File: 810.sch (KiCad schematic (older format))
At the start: 327 parts, among them J1 PJ301BM, J10 PJ301BM, J11 PJ301BM, J12 PJ301BM, J13 PJ301BM, J14 PJ301BM, J15 JACK_MONO_SW, J16 PJ301BM, J17 PJ301B, J18 PJ301B, J2 PJ301BM, J3 PJ301BM, J4 PJ301B, J5 PJ301B, J6 PJ301BM, J7 PJ301BM, J8 PJ301BM, J9 PJ301BM, P1 CONN_01X08, P2 CONN_02X05, P3 CONN_01X03, P4 CONN_01X08, P5 CONN_01X02, P6 CONN_02X03, Q1 PMBT2369, Q10 2SK208-GR, Q11 2SC4738, Q12 2SA1832, Q13 2SA1832, Q14 2SA1832, Q15 2SC4738, Q2 2SK208-GR, Q3 2SA1618, Q4 2SC4207, Q5 2SK208-GR, Q6 MMBF4391LT1G, Q7 2SA1832, Q8 PMBT2369, Q9 2SK208-GR, SW1 SPDT, SW2 SPDT, SW3 BF3-1050, SW4 SPDT, SW5 DP6T-ALPHA-SR2511, U1 TL072-, U10 TL072-, U11 TL072-, U12 TA75S558F, U13 TA75S558F, U14 TA75S558F, U15 TA75S558F, U16 TA75S558F, U17 CD4052, U18 TA75S558F, U19 TL072-, U2 TL072-, U20 CD4013, U21 TA75S558F, U3 TL072-, U4 CD40106, U5 CD4027, U6 LM13700, U7 LM13700, U8 LM13700, U9 TL072-

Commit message: bit of tweaking. ready to order
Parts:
- TC1: footprint MyModules:SM0805-HAND -> MyModules:SM0603-R-JRL
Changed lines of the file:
@@
 F 0 "TC1" H 9800 3850 50  0000 C CNN
 F 1 "1K 3300ppm/K" H 9350 3800 50  0000 C CNN
-F 2 "MyModules:SM0805-HAND" H 9675 3975 60  0001 C CNN
+F 2 "MyModules:SM0603-R-JRL" H 9675 3975 60  0001 C CNN
 F 3 "" H 9675 3975 60  0000 C CNN
 	1    9675 3975

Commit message: added readme, updated schematic based on 4layer build
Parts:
- R3: value 2.2K -> 220
- R55: value 22K -> 1K
- R59: value 1meg -> 470K
- R91: value 15K -> 10K
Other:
- note added: "0.1%"
- note added: "1M?"
- note added: "220R = 9 mA"
- note added: "9.1K? - need a bit more +ve offset\nto prevent clipping in CD4052 (-5V MAX)"
- note added: "DELETE R136"
- note added: "R91 CHANGED BACK\nTO 10K - TOO MUCH GAIN\nCAUSED CLIPPING"
- note removed: "330R?"
- note removed: "CHANGE R88 to 47K?"
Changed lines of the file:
@@
 P 16875 3175
 F 0 "R91" V 16950 3350 50  0000 C CNN
-F 1 "15K" V 16925 3000 50  0000 C CNN
+F 1 "10K" V 16925 3000 50  0000 C CNN
 F 2 "MyModules:SM0603-R-JRL" H 16875 3175 60  0001 C CNN
 F 3 "" H 16875 3175 60  0001 C CNN
@@
 P 1750 3650
 F 0 "R3" V 1830 3650 50  0000 C CNN
-F 1 "2.2K" V 1650 3650 50  0000 C CNN
+F 1 "220" V 1650 3650 50  0000 C CNN
 F 2 "MyModules:SM0603-R-JRL" H 1750 3650 60  0001 C CNN
 F 3 "" H 1750 3650 60  0001 C CNN
@@
 P 11875 7975
 F 0 "R55" V 11955 7975 50  0000 C CNN
-F 1 "22K" V 11775 7975 50  0000 C CNN
+F 1 "1K" V 11775 7975 50  0000 C CNN
 F 2 "MyModules:SM0603-R-JRL" H 11875 7975 60  0001 C CNN
 F 3 "" H 11875 7975 60  0001 C CNN
@@
 P 12175 6275
 F 0 "R59" V 12255 6275 50  0000 C CNN
-F 1 "1meg" V 12075 6275 50  0000 C CNN
+F 1 "470K" V 12075 6275 50  0000 C CNN
 F 2 "MyModules:SM0603-R-JRL" H 12175 6275 60  0001 C CNN
 F 3 "" H 12175 6275 60  0001 C CNN
@@
 Text Notes 16900 5950 0    60   ~ 0
 R95 CHANGED TO 15K
-Text Notes 16425 3325 0    60   ~ 0
-R91 CHANGED TO 15K
 Text Notes 15225 15875 0    60   ~ 0
 CHANGE R73 to 150K
@@
 Text Notes 15275 5575 2    60   ~ 0
 DELETE TRIMMER?
-Text Notes 16075 16575 0    60   ~ 0
-CHANGE R88 to 47K?
 Text Notes 14350 3000 0    60   ~ 0
 DELETE OR\nREDUCE C14
@@
 	23625 6300 23675 6300
 Connection ~ 23650 6300
-Text Notes 1650 3875 0    60   ~ 0
-330R?
 $Comp
 L +10V #PWR0220
@@
 	1    0    0    -1
 $EndComp
+Text Notes 1250 3875 0    60   ~ 0
+220R = 9 mA
+Text Notes 5900 2025 0    60   ~ 0
+0.1%
+Text Notes 5900 5100 0    60   ~ 0
+0.1%
+Text Notes 16125 18725 0    60   ~ 0
+DELETE R136
+Text Notes 11200 2925 0    60   ~ 0
+1M?
+Text Notes 16425 3325 0    60   ~ 0
+R91 CHANGED TO 15K
+Text Notes 17500 3500 0    60   ~ 0
+R91 CHANGED BACK\nTO 10K - TOO MUCH GAIN\nCAUSED CLIPPING
+Text Notes 16375 2575 0    60   ~ 0
+9.1K? - need a bit more +ve offset\nto prevent clipping in CD4052 (-5V MAX)
 $EndSCHEMATC

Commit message: couple of notes added and changed in schematic
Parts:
- added R?: 270K, MyModules:SM0603-R-JRL, symbol R_US
- R137: value 15K -> 330
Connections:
- net at R99.1, VR24.2: now also R?.2
- net at R137.2, U10.3 (+): now also R?.1
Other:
- note added: "220R"
- note added: "CHANGE R15 to 220K?"
- note added: "DELETE R106"
- note added: "OPA2180 low drift?\nTried, works.\nNeeds new footprint"
- note removed: "100K?"
- note removed: "100R?"
- note removed: "CHANGE R15 to 180K"
- note removed: "Does CV summer need conditioned rails?\nUse a rail-rail opamp here?"

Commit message: changed a couple of schematic notes
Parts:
- gave numbers to parts that had none: 1

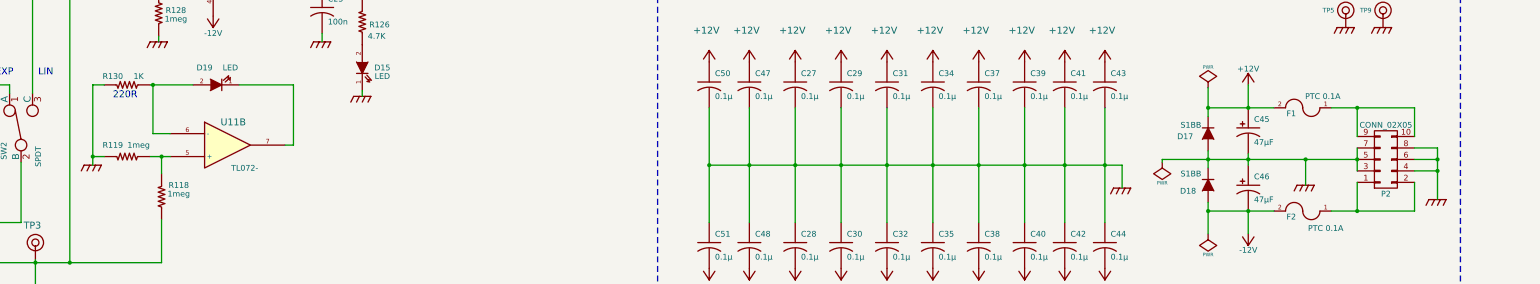
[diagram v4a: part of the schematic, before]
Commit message: separate LED ground path
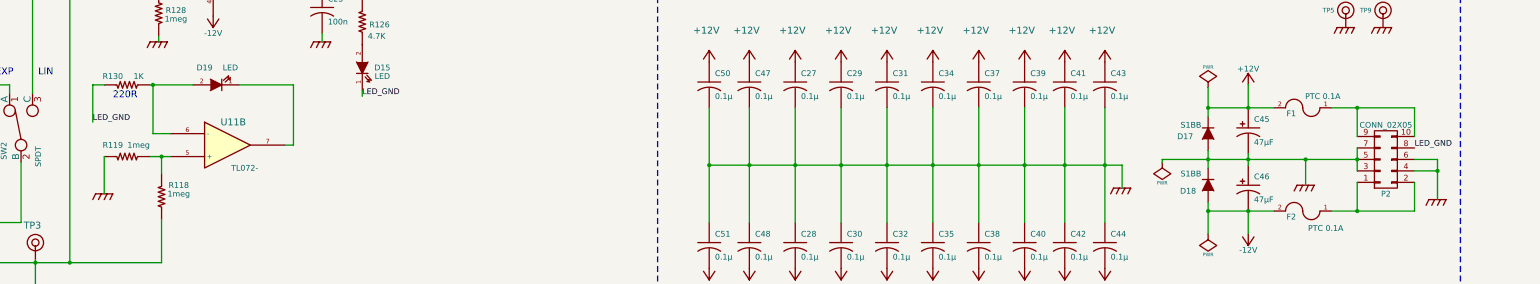
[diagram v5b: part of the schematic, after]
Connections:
- net GND: no longer D15.1 (K), P2.8 (P8), R130.1
- new net LED_GND: D15.1 (K), P2.8 (P8), R130.1
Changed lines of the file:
@@
 Connection ~ 31725 18300
 Wire Wire Line
-	32225 17750 32425 17750
-Wire Wire Line
-	32425 17750 32425 18200
-Wire Wire Line
 	32225 17850 32425 17850
-Connection ~ 32425 17850
 Wire Wire Line
 	32225 17950 32425 17950
@@
 Wire Wire Line
 	23050 16450 23050 16400
-$Comp
-L GND_R #PWR0199
-U 1 1 5A61093A
-P 23050 17300
-F 0 "#PWR0199" H 23050 17300 30  0001 C CNN
-F 1 "GND_R" H 23050 17200 30  0001 C CNN
-F 2 "" H 23050 17300 60  0000 C CNN
-F 3 "" H 23050 17300 60  0000 C CNN
-	1    23050 17300
-	1    0    0    -1
-$EndComp
 Wire Wire Line
 	23050 17250 23050 17300
@@
 Wire Wire Line
 	20800 17200 20700 17200
-Wire Wire Line
-	20700 17200 20700 17900
-Wire Wire Line
-	20700 17825 20800 17825
-$Comp
-L GND_R #PWR0200
-U 1 1 5A61BC58
-P 20700 17900
-F 0 "#PWR0200" H 20700 17900 30  0001 C CNN
-F 1 "GND_R" H 20700 17800 30  0001 C CNN
-F 2 "" H 20700 17900 60  0000 C CNN
-F 3 "" H 20700 17900 60  0000 C CNN
-	1    20700 17900
-	1    0    0    -1
-$EndComp
-Connection ~ 20700 17825
 Wire Wire Line
 	21300 17975 21300 17825
@@
 Text Notes 18600 12600 0    60   ~ 0
 DELETE R106
+Wire Wire Line
+	32425 17850 32425 18200
+Text Label 32225 17750 0    50   ~ 0
+LED_GND
+Text Label 23050 17300 0    50   ~ 0
+LED_GND
+$Comp
+L GND_R #PWR?
+U 1 1 5BAFA430
+P 20800 18150
+F 0 "#PWR?" H 20800 18150 30  0001 C CNN
+F 1 "GND_R" H 20800 18050 30  0001 C CNN
+F 2 "" H 20800 18150 60  0000 C CNN
+F 3 "" H 20800 18150 60  0000 C CNN
+	1    20800 18150
+	1    0    0    -1
+$EndComp
+Wire Wire Line
+	20800 17825 20800 18150
+Text Label 20700 17525 0    50   ~ 0
+LED_GND
+Wire Wire Line
+	20700 17200 20700 17525
 $EndSCHEMATC

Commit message: meh. gonna change matched pair and repanelize
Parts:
- R49: value 1.5M -> 1meg
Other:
- note added: "1 meg for\nIref = 10µA"
- note removed: "1M?"
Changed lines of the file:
@@
 P 10975 2875
 F 0 "R49" H 10850 2825 50  0000 C CNN
-F 1 "1.5M" H 10850 2900 50  0000 C CNN
+F 1 "1meg" H 10850 2900 50  0000 C CNN
 F 2 "MyModules:SM0603-R-JRL" H 10975 2875 60  0001 C CNN
 F 3 "" H 10975 2875 60  0001 C CNN
@@
 Text Notes 16125 18725 0    60   ~ 0
 DELETE R136
-Text Notes 11200 2925 0    60   ~ 0
-1M?
+Text Notes 10925 2950 2    60   ~ 0
+1 meg for\nIref = 10µA
 Text Notes 16425 3325 0    60   ~ 0
 R91 CHANGED TO 15K

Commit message: updated matched pair to PMP4201
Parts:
- added Q16: PMP4201, TO_SOT_Packages_SMD:SOT-666, symbol PMP4201
- added R151, R89: 16.9, MyModules:SM0603-R-JRL, symbol R_US
- added TC1: 500R ±3850ppm/°C, Resistors_SMD:R_0805, symbol R_TEMPCO
- R37: value 91K -> 82K
- R47: value 56K -> 27K
- SW5: symbol DP6T-ALPHA-SR2511 -> DP6T-ALPHA-SR2511-RESCUE-810
- TC2: renamed from TC1; value 1K 3300ppm/K -> 500R ±3850ppm/°C; footprint MyModules:SM0603-R-JRL -> Resistors_SMD:R_0805
- U1: value TL072- -> OPA2180
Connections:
- net GND: now also Q16.2 (B), R151.1, R89.1; no longer TC2.2
- net B: now reaches Q4.1 (B), R47.2, TC2.1
- net B: now also Q16.1 (B), TC1.1
- net C1: now reaches C9.1, Q4.5 (C), R49.1, U1.6 (-)
- net C1: now also Q16.6 (C)
- net E: now reaches Q4.2 (E), Q4.2 (E), R51.2
- net E: now also Q16.4 (E), Q16.5 (E)
- net C2: now reaches Q4.4 (C), R53.1, U2.2 (-)
- net C2: now also Q16.3 (C)
- new net: R151.2, TC2.2
- new net: R89.2, TC1.2
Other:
- note removed: "CHANGE TO 0603\nFOR PRODUCTION"
- note removed: "OPA2180 low drift?\nTried, works.\nNeeds new footprint"
- note removed: "USE +10V\nREF HERE?"
- note removed: "or J112?"
- moved on the sheet: Q4A, Q4B, TC2

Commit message: reverted back to 2SC4207 and single tempco in divider
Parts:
- removed C14: 10n, MyModules:SM0603-C-JRL, symbol C_US
- removed Q16: PMP4201, TO_SOT_Packages_SMD:SOT-666, symbol PMP4201
- removed R151, R89: 16.9, MyModules:SM0603-R-JRL, symbol R_US
- removed TC2: 500R ±3850ppm/°C, Resistors_SMD:R_0805, symbol R_TEMPCO
- TC1: value 500R ±3850ppm/°C -> 1K 3300ppm/°C; footprint Resistors_SMD:R_0805 -> MyModules:SM0603-R-YAGEO
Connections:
- net GND: now also TC1.2
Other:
- note removed: "DELETE OR\nREDUCE C14"
- moved on the sheet: Q4A, Q4B
